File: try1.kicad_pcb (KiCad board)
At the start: 2 copper layers, 175.3 x 119.4 mm, 33 parts, among them J10 Archon-connector-modules-Driv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, J11 Archon-connector-modules-Driv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, J2 Archon-connector-modules-Heat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, J21 DB37, J22 DB37, J3 Archon-connector-modules-Driv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, J31 DB9, J4 Archon-connector-modules-LVBi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, J41 CONN_DVI, J5 Archon-connector-modules-ADC, J6 Archon-connector-modules-ADC, J7 Archon-connector-modules-ADC, J8 Archon-connector-modules-ADC, J9 Archon-connector-modules-HVBi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, P1 CONN_02X02

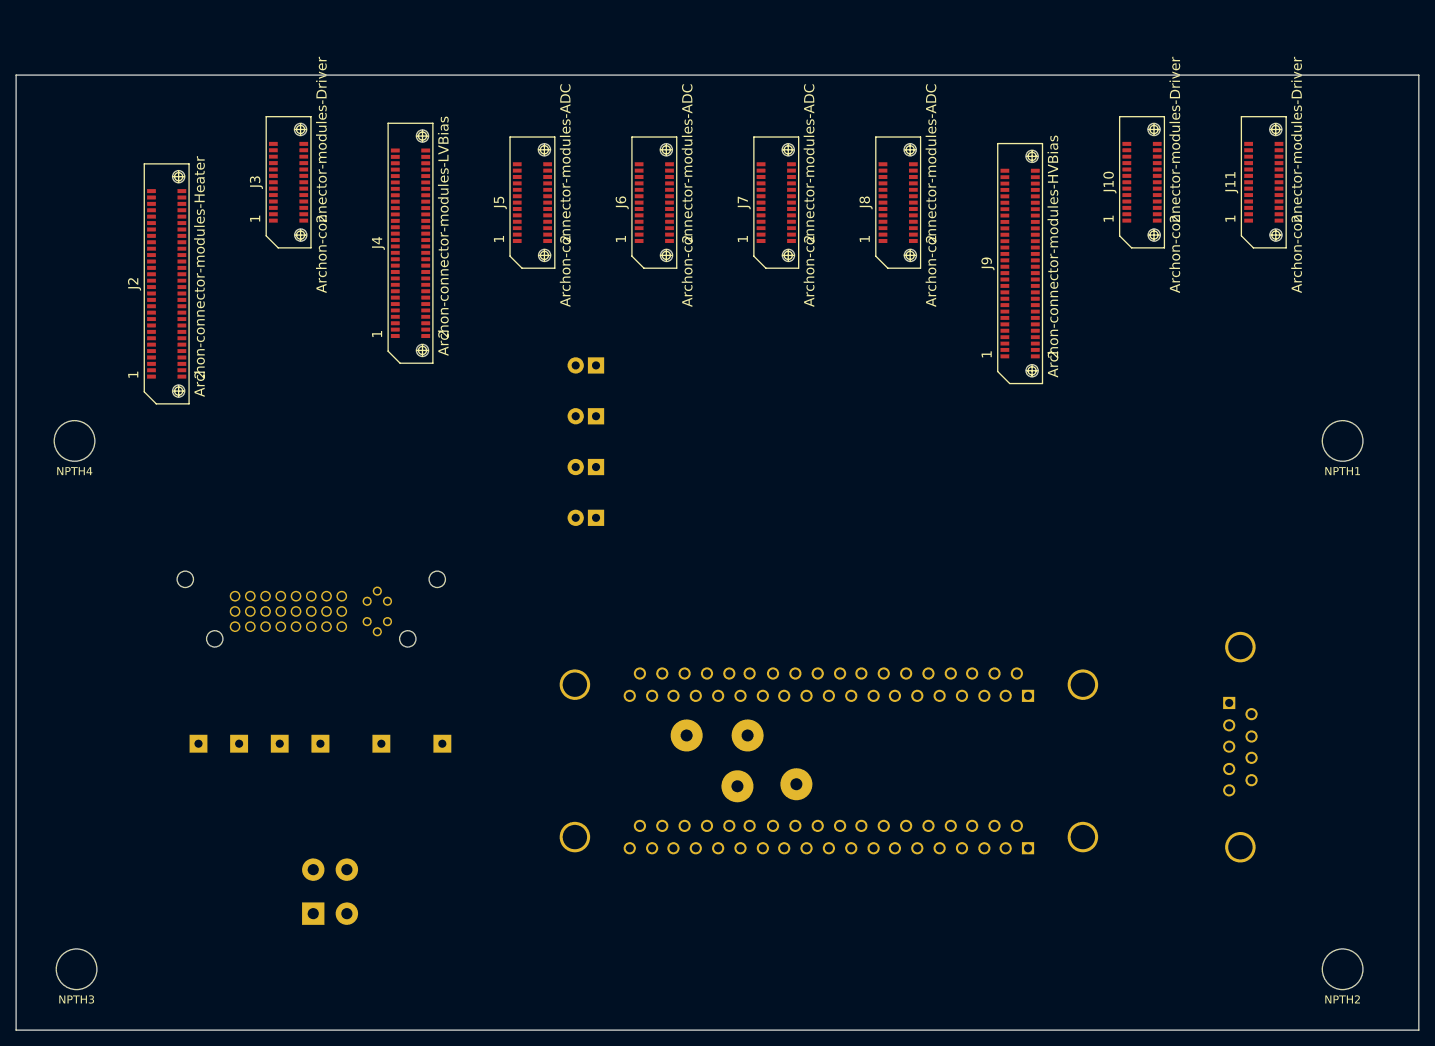
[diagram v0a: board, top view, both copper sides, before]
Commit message: Place GND Plane Before Freeroute
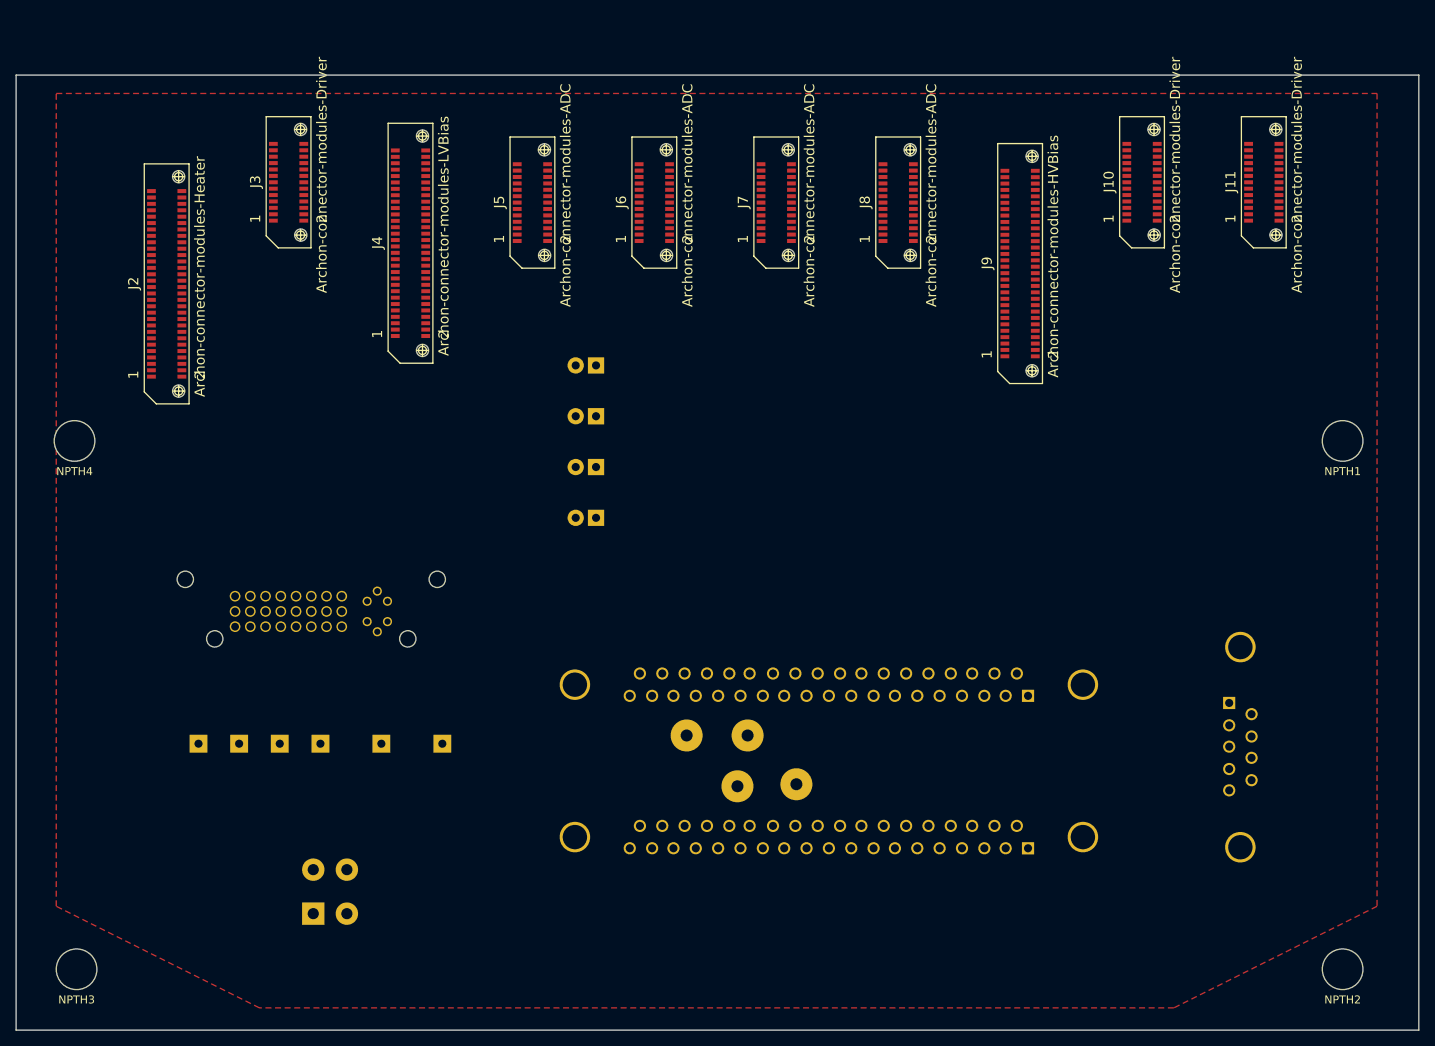
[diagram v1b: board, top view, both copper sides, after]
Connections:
- J2 pad 59: Net-(J2-Pad59) -> /GND
- J2 pad 60: Net-(J2-Pad60) -> /GND
- J4 pad 59: Net-(J4-Pad59) -> /GND
- J4 pad 60: Net-(J4-Pad60) -> /GND
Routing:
- added copper zone on F.Cu, net /GND

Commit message: Reroute After GND Plane, Fat Heater Traces
I used freerouter after creating the GND plane, and that just caused it
not to connect any of the GND pins.  That made the resulting traces better
(fewer vias), it didn't connect some pins at all.

Also, I figured out how to change the trace width for the heater circuit.
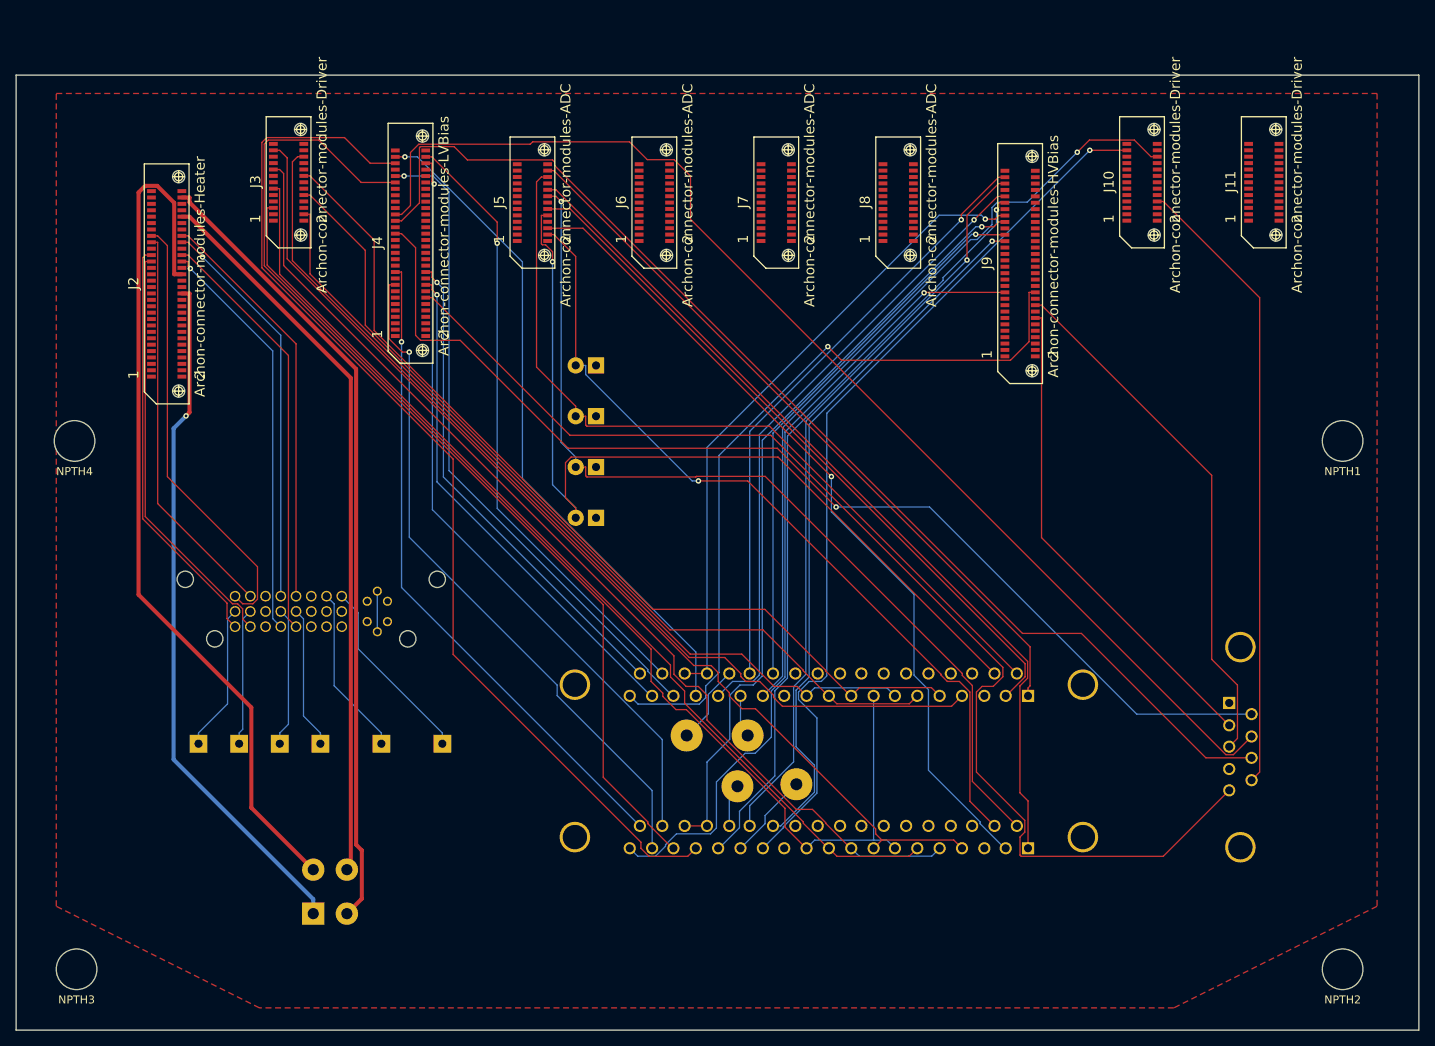
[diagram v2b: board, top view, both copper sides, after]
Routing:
- net LV4_7: track 0.00 -> 150.5 mm
- net LED_+15V: track 0.00 -> 149.3 mm
- net LV4_8: track 0.00 -> 146.8 mm
- net DRV3_CH8: track 0.00 -> 139.5 mm
- net LV4_9: track 0.00 -> 138.3 mm, vias 0 -> 1
- net LV4_2: track 0.00 -> 133.8 mm
- net DRV3_CH2: track 0.00 -> 132.3 mm
- net DRV3_CH4: track 0.00 -> 129.2 mm
- net LV4_4: track 0.00 -> 128.1 mm
- net DRV3_CH6: track 0.00 -> 123.6 mm
- net DRV3_CH1: track 0.00 -> 121.7 mm
- net /OUT_LR_GND: track 0.00 -> 117.5 mm, vias 0 -> 1
- net DRV3_CH3: track 0.00 -> 113.9 mm
- net /OUT_LL_GND: track 0.00 -> 113.1 mm, vias 0 -> 1
- net DRV10_CH2: track 0.00 -> 111.6 mm, vias 0 -> 1
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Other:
- net class oldHeater added: clearance 0.254, trace_width 0.508, via_dia 0.6858, via_drill 0.3302

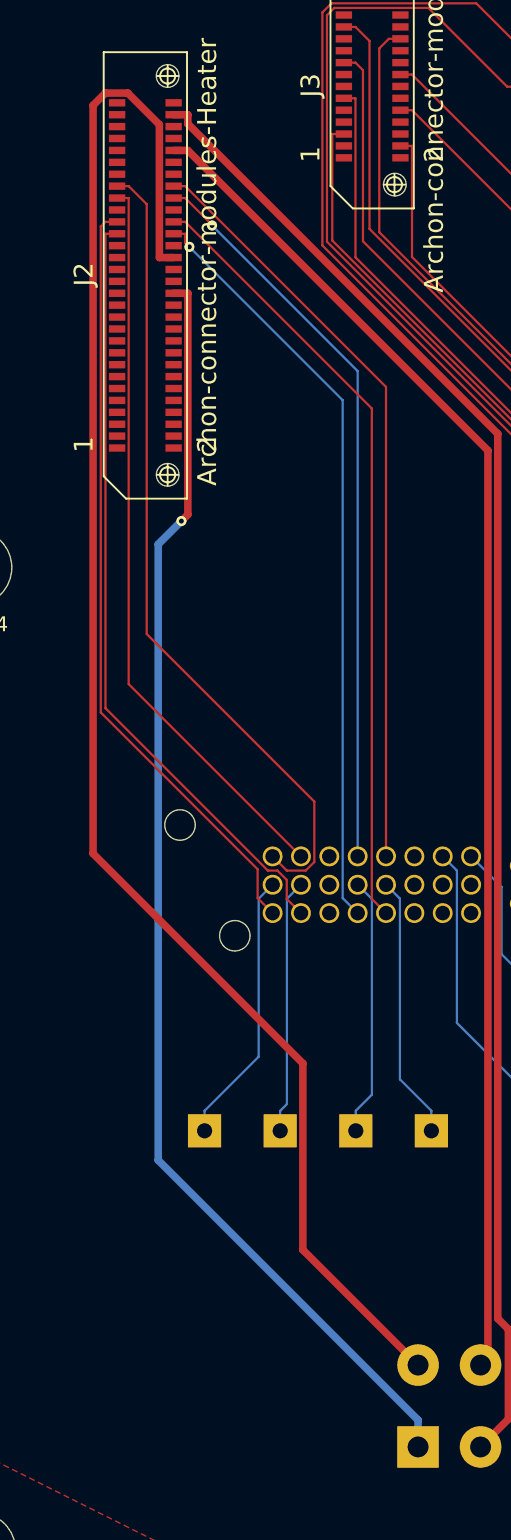
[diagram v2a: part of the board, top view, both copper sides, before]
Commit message: WIP: FreeRouter Fixes
Fixed the heater power traces a little bit, manually.  I think I see how
this could work, now.

Still TODO:
  Check and fix all ground connections
  Eliminate isolated fill areas
  Double check connetions
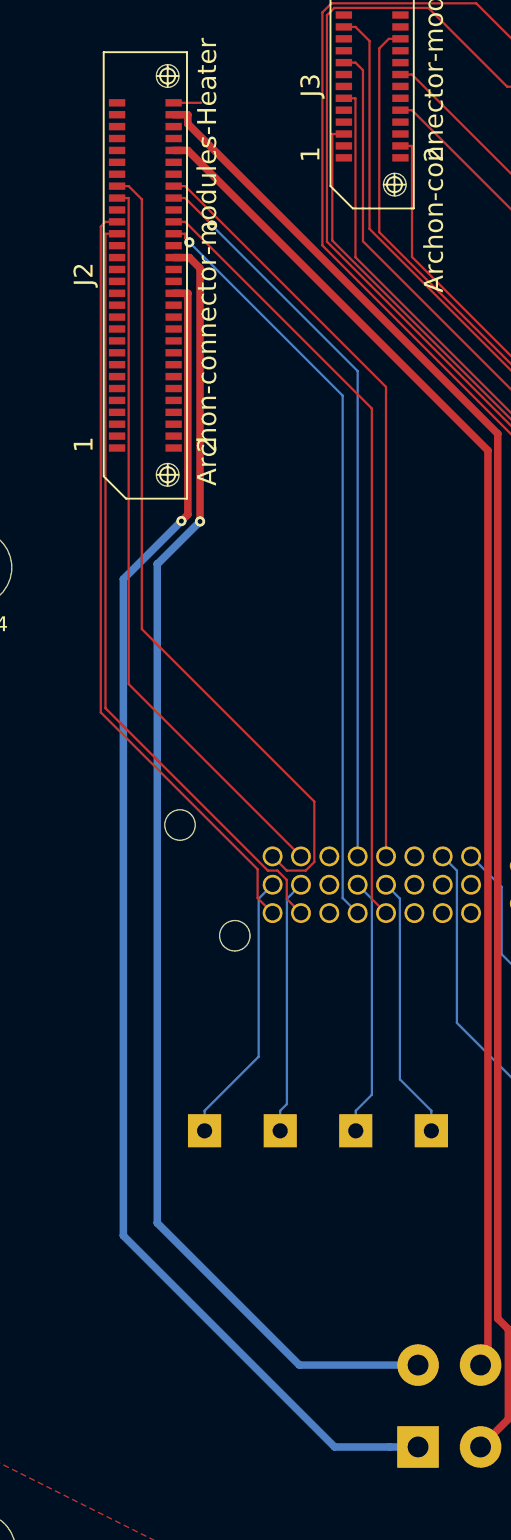
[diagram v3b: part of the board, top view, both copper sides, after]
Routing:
- net HEATER1_AN: track 109.3 -> 88.9 mm, vias 0 -> 1
- net HEATER1_AP: track 86.5 -> 91.8 mm
- net /GND: track 0.00 -> 1.83 mm
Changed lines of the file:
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@@
   (general
     (links 118)
-    (no_connects 26)
-    (area 45.767299 23.087299 221.132701 142.492701)
+    (no_connects 25)
+    (area 41.951046 18.373109 222.731954 142.492701)
     (thickness 1.6)
     (drawings 7)
-    (tracks 620)
+    (tracks 624)
     (zones 0)
     (modules 33)
@@
   (target plus (at 52.07 99.06) (size 5) (width 0.15) (layer Edge.Cuts))
   (target plus (at 52.07 35.56) (size 5) (width 0.15) (layer Edge.Cuts))
+  (segment (start 66.49992 37.60236) (end 68.31564 37.60236) (width 0.1524) (layer F.Cu) (net 23))
+  (segment (start 68.31564 37.60236) (end 68.326 37.592) (width 0.1524) (layer F.Cu) (net 23))
+  (segment (start 81.0179 127.922) (end 82.9259 127.922) (width 0.508) (layer B.Cu) (net 27))
+  (segment (start 77.314354 127.922) (end 81.0179 127.922) (width 0.508) (layer B.Cu) (net 27))
+  (segment (start 63.121124 69.607876) (end 63.121124 113.72877) (width 0.508) (layer B.Cu) (net 27))
+  (segment (start 67.0225 65.7065) (end 63.121124 69.607876) (width 0.508) (layer B.Cu) (net 27))
+  (segment (start 63.121124 113.72877) (end 77.314354 127.922) (width 0.508) (layer B.Cu) (net 27))
+  (segment (start 66.4999 50.3989) (end 67.4565 50.3989) (width 0.508) (layer F.Cu) (net 27))
+  (segment (start 67.4565 50.3989) (end 67.4565 65.2725) (width 0.508) (layer F.Cu) (net 27))
+  (segment (start 67.4565 65.2725) (end 67.0225 65.7065) (width 0.508) (layer F.Cu) (net 27))
   (via (at 67.0225 65.7065) (size 0.6858) (layers F.Cu B.Cu) (net 27))
-  (segment (start 67.4565 65.2725) (end 67.0225 65.7065) (width 0.508) (layer F.Cu) (net 27))
-  (segment (start 67.4565 50.3989) (end 67.4565 65.2725) (width 0.508) (layer F.Cu) (net 27))
-  (segment (start 65.4631 108.6525) (end 82.9259 126.1153) (width 0.508) (layer B.Cu) (net 27))
-  (segment (start 65.4631 67.2659) (end 65.4631 108.6525) (width 0.508) (layer B.Cu) (net 27))
-  (segment (start 67.0225 65.7065) (end 65.4631 67.2659) (width 0.508) (layer B.Cu) (net 27))
-  (segment (start 66.4999 50.3989) (end 67.4565 50.3989) (width 0.508) (layer F.Cu) (net 27))
-  (segment (start 82.9259 127.922) (end 82.9259 126.1153) (width 0.508) (layer B.Cu) (net 27))
-  (segment (start 75.1844 114.6805) (end 82.9259 122.422) (width 0.508) (layer F.Cu) (net 33))
-  (segment (start 75.1844 102.1478) (end 75.1844 114.6805) (width 0.508) (layer F.Cu) (net 33))
-  (segment (start 61.0867 88.0501) (end 75.1844 102.1478) (width 0.508) (layer F.Cu) (net 33))
-  (segment (start 61.0867 37.772) (end 61.0867 88.0501) (width 0.508) (layer F.Cu) (net 33))
-  (segment (start 61.912 36.9467) (end 61.0867 37.772) (width 0.508) (layer F.Cu) (net 33))
-  (segment (start 63.4206 36.9467) (end 61.912 36.9467) (width 0.508) (layer F.Cu) (net 33))
-  (segment (start 65.5433 39.0694) (end 63.4206 36.9467) (width 0.508) (layer F.Cu) (net 33))
-  (segment (start 65.5433 48.0011) (end 65.5433 39.0694) (width 0.508) (layer F.Cu) (net 33))
-  (segment (start 66.4999 48.0011) (end 65.5433 48.0011) (width 0.508) (layer F.Cu) (net 33))
+  (segment (start 82.9259 122.422) (end 74.9494 122.422) (width 0.508) (layer B.Cu) (net 33))
+  (segment (start 74.9494 122.422) (end 65.398649 112.871249) (width 0.508) (layer B.Cu) (net 33))
+  (segment (start 65.398649 112.871249) (end 65.398649 68.586351) (width 0.508) (layer B.Cu) (net 33))
+  (segment (start 65.398649 68.586351) (end 65.424049 68.586351) (width 0.508) (layer B.Cu) (net 33))
+  (segment (start 65.424049 68.586351) (end 68.2752 65.7352) (width 0.508) (layer B.Cu) (net 33))
+  (segment (start 68.2752 65.7352) (end 68.2752 48.71849) (width 0.508) (layer F.Cu) (net 33))
+  (segment (start 68.2752 48.71849) (end 67.55783 48.00112) (width 0.508) (layer F.Cu) (net 33))
+  (via (at 68.2752 65.7352) (size 0.6858) (drill 0.3302) (layers F.Cu B.Cu) (net 33))
+  (segment (start 66.49992 48.00112) (end 67.55783 48.00112) (width 0.508) (layer F.Cu) (net 33))
+  (segment (start 67.55783 48.00112) (end 67.56271 48.006) (width 0.508) (layer F.Cu) (net 33))
   (segment (start 74.1045 91.0971) (end 75.057 92.0496) (width 0.1524) (layer F.Cu) (net 36))
   (segment (start 74.1045 89.8211) (end 74.1045 91.0971) (width 0.1524) (layer F.Cu) (net 36))
   (segment (start 73.4755 89.1921) (end 74.1045 89.8211) (width 0.1524) (layer F.Cu) (net 36))
+  (segment (start 61.9213 46.4009) (end 61.9213 78.281) (width 0.1524) (layer F.Cu) (net 36))
+  (segment (start 61.9213 78.281) (end 72.8324 89.1921) (width 0.1524) (layer F.Cu) (net 36))
   (segment (start 72.8324 89.1921) (end 73.4755 89.1921) (width 0.1524) (layer F.Cu) (net 36))
-  (segment (start 61.9213 78.281) (end 72.8324 89.1921) (width 0.1524) (layer F.Cu) (net 36))
-  (segment (start 61.9213 46.4009) (end 61.9213 78.281) (width 0.1524) (layer F.Cu) (net 36))
   (segment (start 62.7001 46.4009) (end 61.9213 46.4009) (width 0.1524) (layer F.Cu) (net 36))
-  (via (at 67.5587 47.2809) (size 0.6858) (layers F.Cu B.Cu) (net 37))
-  (segment (start 77.859 57.5812) (end 67.5587 47.2809) (width 0.1524) (layer B.Cu) (net 37))
-  (segment (start 77.859 91.0416) (end 77.859 57.5812) (width 0.1524) (layer B.Cu) (net 37))
+  (segment (start 66.4999 46.4009) (end 67.2787 46.4009) (width 0.1524) (layer F.Cu) (net 37))
+  (segment (start 67.2787 46.4009) (end 67.2787 46.6961) (width 0.1524) (layer F.Cu) (net 37))
+  (segment (start 67.2787 46.6961) (end 67.5587 46.9761) (width 0.1524) (layer F.Cu) (net 37))
+  (via (at 67.5587 46.9761) (size 0.6858) (layers F.Cu B.Cu) (net 37))
   (segment (start 78.867 92.0496) (end 77.859 91.0416) (width 0.1524) (layer B.Cu) (net 37))
-  (segment (start 67.2787 47.0009) (end 67.5587 47.2809) (width 0.1524) (layer F.Cu) (net 37))
-  (segment (start 67.2787 46.4009) (end 67.2787 47.0009) (width 0.1524) (layer F.Cu) (net 37))
-  (segment (start 66.4999 46.4009) (end 67.2787 46.4009) (width 0.1524) (layer F.Cu) (net 37))
+  (segment (start 77.859 91.0416) (end 77.859 57.2764) (width 0.1524) (layer B.Cu) (net 37))
+  (segment (start 77.859 57.2764) (end 67.5587 46.9761) (width 0.1524) (layer B.Cu) (net 37))
   (segment (start 72.144 91.0416) (end 73.152 92.0496) (width 0.1524) (layer F.Cu) (net 38))
+  (segment (start 61.6048 78.5644) (end 72.144 89.1036) (width 0.1524) (layer F.Cu) (net 38))
+  (segment (start 61.9213 45.6008) (end 61.6048 45.9173) (width 0.1524) (layer F.Cu) (net 38))
   (segment (start 72.144 89.1036) (end 72.144 91.0416) (width 0.1524) (layer F.Cu) (net 38))
-  (segment (start 61.6048 78.5644) (end 72.144 89.1036) (width 0.1524) (layer F.Cu) (net 38))
   (segment (start 61.6048 45.9173) (end 61.6048 78.5644) (width 0.1524) (layer F.Cu) (net 38))
-  (segment (start 61.9213 45.6008) (end 61.6048 45.9173) (width 0.1524) (layer F.Cu) (net 38))
   (segment (start 62.7001 45.6008) (end 61.9213 45.6008) (width 0.1524) (layer F.Cu) (net 38))
   (segment (start 79.8195 91.0971) (end 80.772 92.0496) (width 0.1524) (layer F.Cu) (net 39))
@@
   (segment (start 75.954 88.6156) (end 75.3775 89.1921) (width 0.1524) (layer F.Cu) (net 44))
   (segment (start 75.954 84.5561) (end 75.954 88.6156) (width 0.1524) (layer F.Cu) (net 44))
-  (segment (start 64.6921 73.2942) (end 75.954 84.5561) (width 0.1524) (layer F.Cu) (net 44))
-  (segment (start 64.6921 44.4137) (end 64.6921 73.2942) (width 0.1524) (layer F.Cu) (net 44))
-  (segment (start 63.4789 43.2005) (end 64.6921 44.4137) (width 0.1524) (layer F.Cu) (net 44))
+  (segment (start 64.3619 72.964) (end 75.954 84.5561) (width 0.1524) (layer F.Cu) (net 44))
+  (segment (start 64.3619 44.0835) (end 64.3619 72.964) (width 0.1524) (layer F.Cu) (net 44))
+  (segment (start 63.4789 43.2005) (end 64.3619 44.0835) (width 0.1524) (layer F.Cu) (net 44))
   (segment (start 62.7001 43.2005) (end 63.4789 43.2005) (width 0.1524) (layer F.Cu) (net 44))
   (segment (start 80.772 56.6938) (end 80.772 88.2396) (width 0.1524) (layer F.Cu) (net 45))
